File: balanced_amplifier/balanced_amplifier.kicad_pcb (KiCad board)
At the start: 2 copper layers, 100 x 100 mm, 128 parts, among them J1 Molex_SL_01x02_Male, J2 Molex_SL_01x02_Male, J3 Molex_SL_01x03_Male, J4 Molex_SL_01x02_Male, J5 Molex_SL_01x02_Male, J6 Molex_SL_01x02_Male, J7 Molex_SL_01x02_Male, U1 LM4562, U2 LM4562, U3 NE5532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

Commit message: update todo (add reminder to consider switching to horizontal connectors)
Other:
- board text added: "TODO Update date silk check pot directions change to horizontal connectors?"
- board text removed: "TODO Update date silk check pot directions"
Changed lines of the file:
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@@
-(kicad_pcb (version 20171130) (host pcbnew 5.1.2)
+(kicad_pcb (version 20171130) (host pcbnew 5.1.4)
   (general
     (thickness 1.6)
@@
     (arrow2b (pts (xy 65.200001 33.8) (xy 65.786422 34.926504)))
   )
-  (gr_text "TODO\nUpdate date silk\ncheck pot directions" (at 213.2 34.3) (layer Cmts.User)
+  (gr_text "TODO\nUpdate date silk\ncheck pot directions\nchange to horizontal connectors?" (at 213.2 34.3) (layer Cmts.User)
     (effects (font (size 1 1) (thickness 0.15)) (justify left))
   )

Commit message: move pots to be 60mm apart
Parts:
- moved RV1 3.54 mm to (93.7, 116.8)
- moved RV2 3.46 mm to (153.7, 116.8)
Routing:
- net Net-(C26-Pad2): track 89.9 -> 132.0 mm
- net Net-(C22-Pad1): track 30.3 -> 64.9 mm
- net Net-(C15-Pad2): track 20.8 -> 37.7 mm
- net Net-(C21-Pad1): track 43.8 -> 60.0 mm
- net Net-(C28-Pad1): track 57.7 -> 45.2 mm
- net Net-(C33-Pad2): track 66.0 -> 60.8 mm
- net Net-(C29-Pad1): track 15.5 -> 18.4 mm
- net Net-(RV1-Pad5): track 16.9 -> 15.0 mm
- net Net-(C7-Pad2): track 27.5 -> 29.3 mm

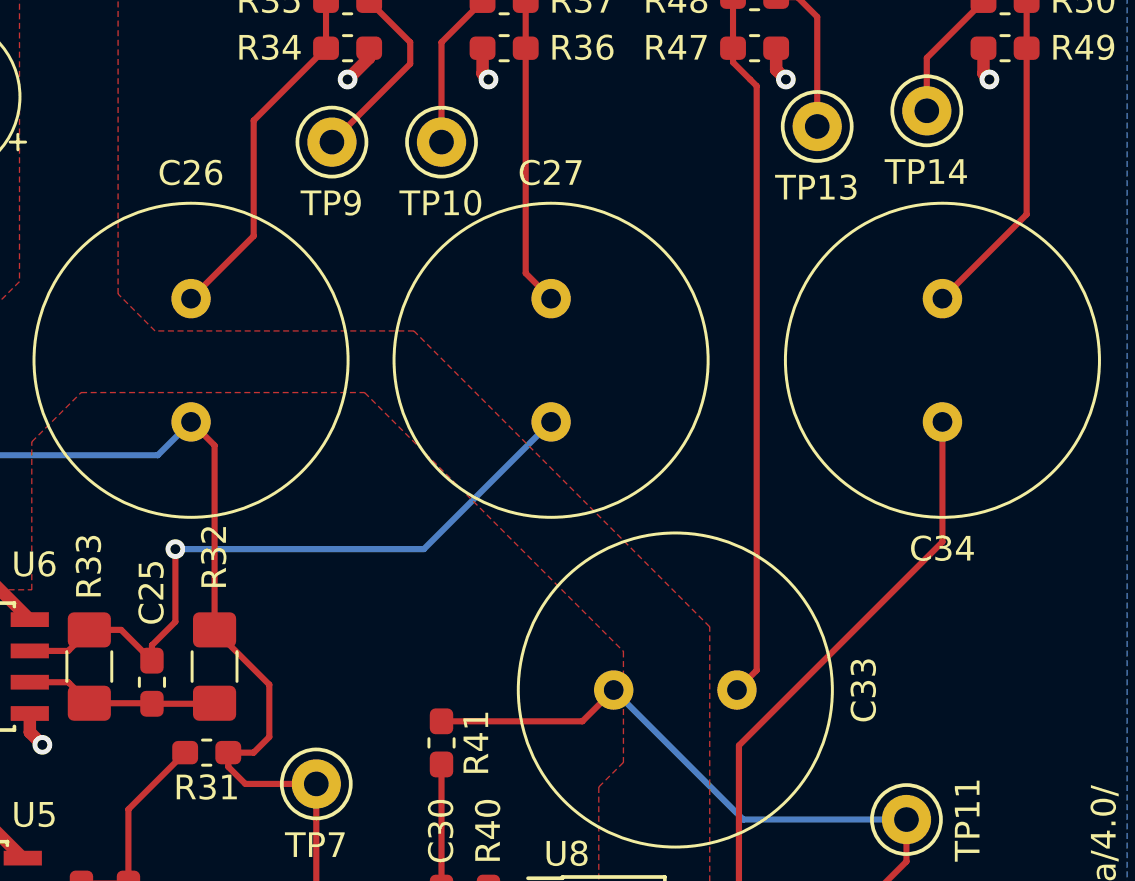
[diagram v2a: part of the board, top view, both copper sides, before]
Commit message: update footprint references for pots and output caps
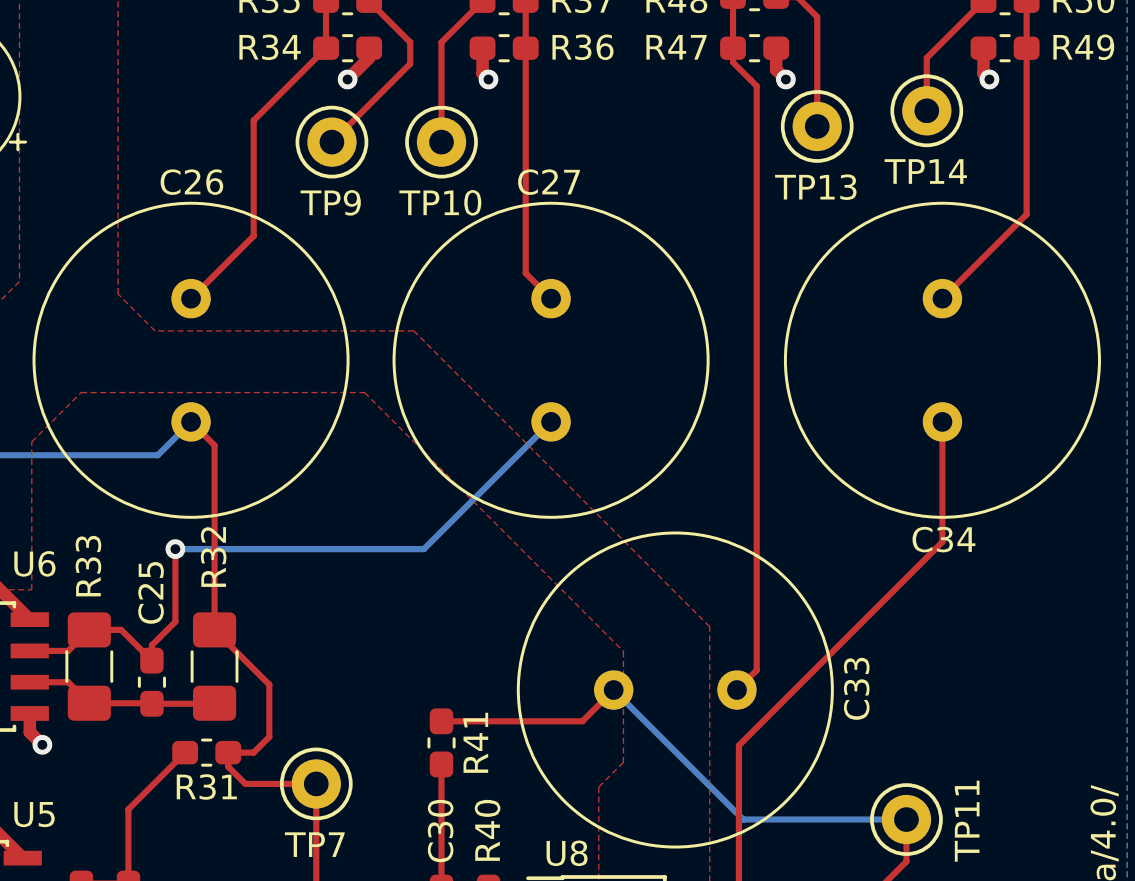
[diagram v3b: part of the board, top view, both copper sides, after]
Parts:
- C26, C27, C33, C34: footprint Capacitor_THT:C_Radial_D12.5mm_H25.0mm_P5.00mm -> Capacitor_THT:C_Radial_D12.5mm_H20.0mm_P5.00mm
- RV1, RV2: footprint Potentiometer_THT_custom:Potentiometer_Bourns_91A2x-x28-xxx_Dual_Horizontal -> Potentiometer_THT_gkeeth:Potentiometer_Bourns_91A2x-x28-xxx_Dual_Horizontal

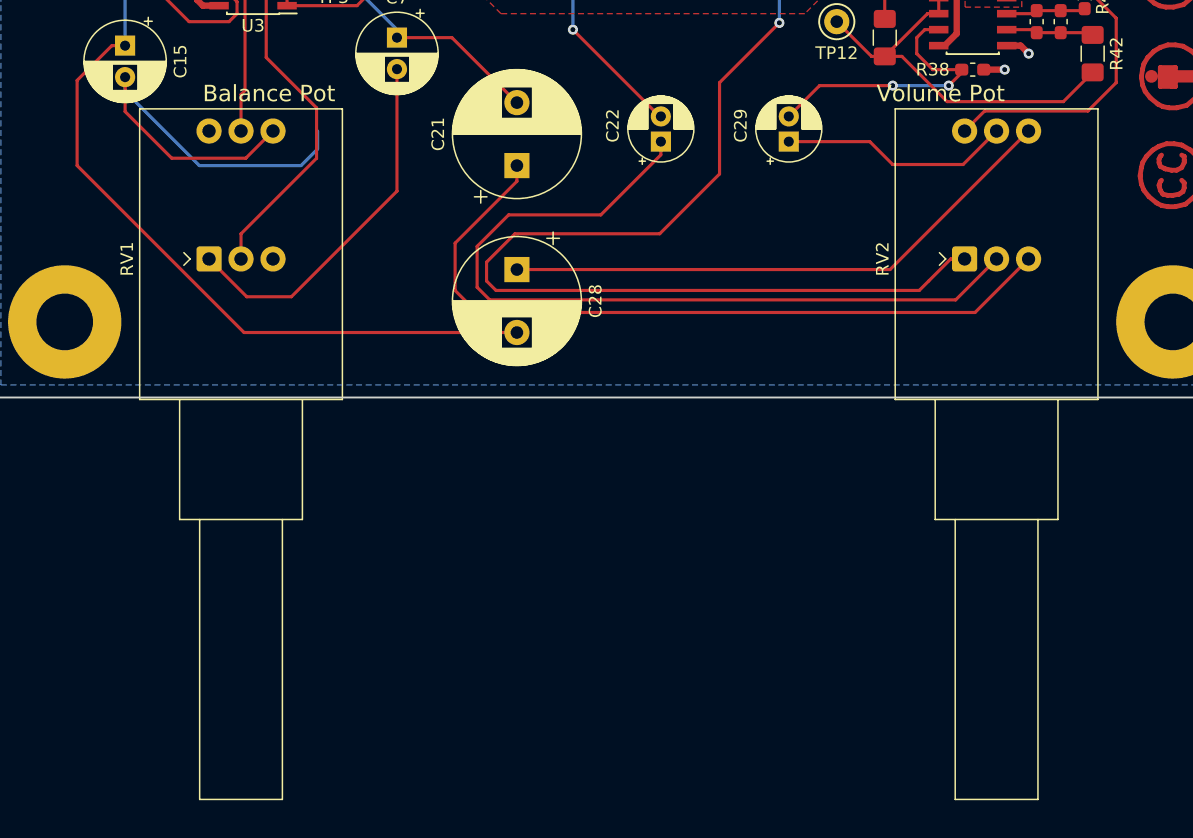
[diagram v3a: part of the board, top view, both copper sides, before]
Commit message: move pots 1mm further beyond board edge
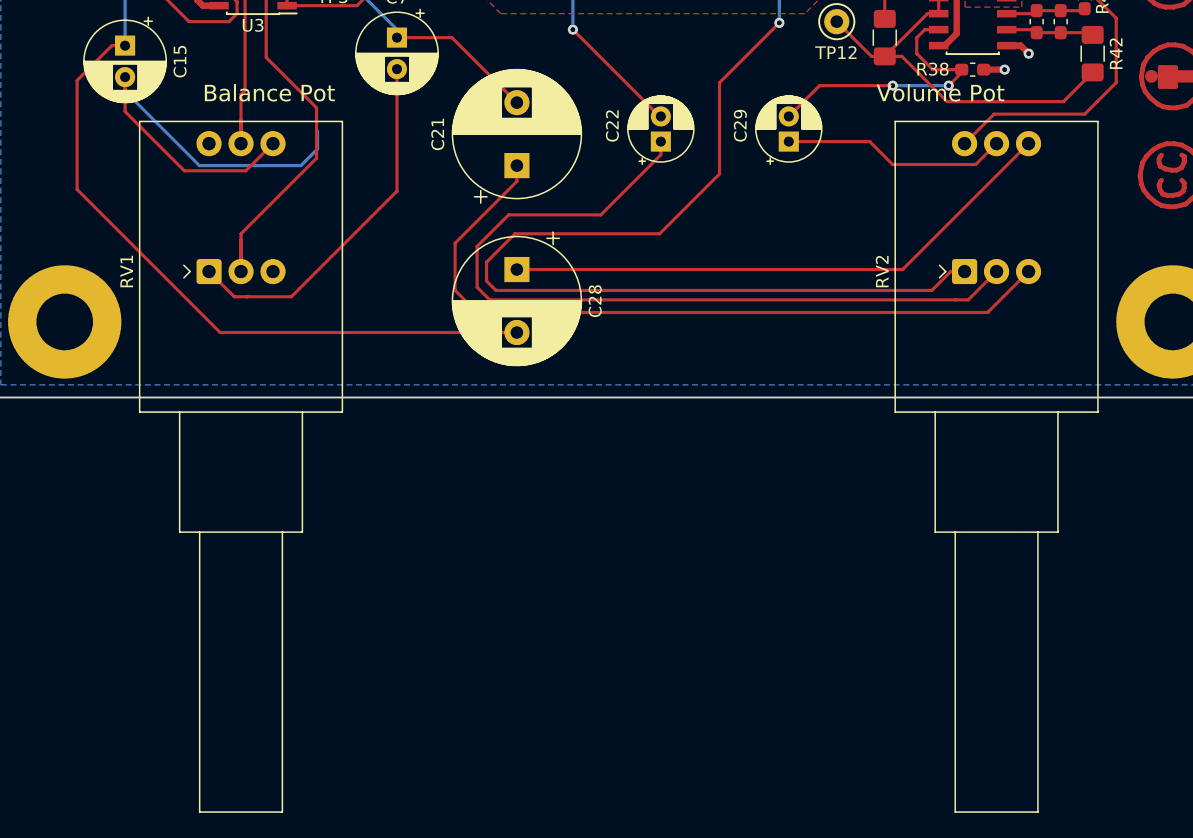
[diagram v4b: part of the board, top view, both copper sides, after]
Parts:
- moved RV1 1.00 mm to (93.7, 117.8)
- moved RV2 1.00 mm to (153.7, 117.8)
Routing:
- net Net-(RV1-Pad2): track 27.8 -> 30.3 mm
- net Net-(RV1-Pad5): track 15.0 -> 16.9 mm
- net /volume_control/left_in: track 74.3 -> 75.4 mm

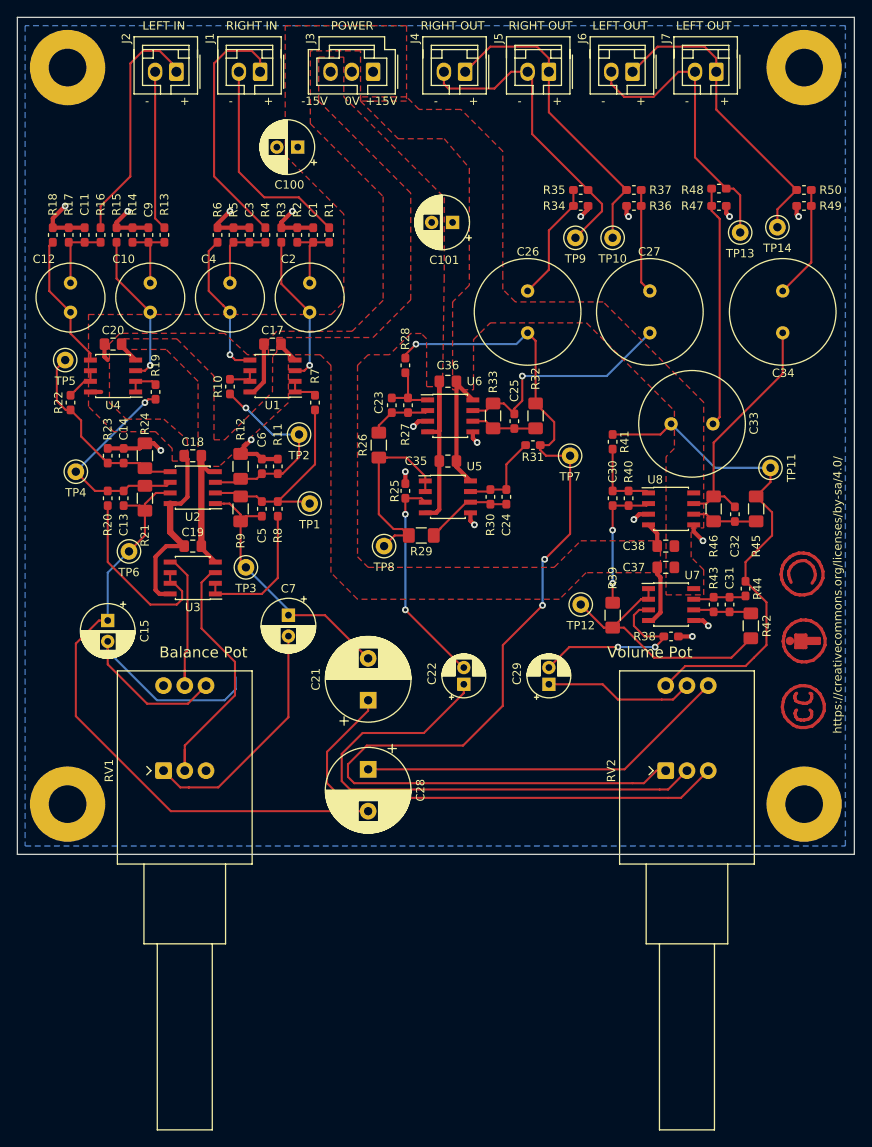
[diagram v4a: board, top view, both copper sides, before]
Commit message: Finalize layout for rev1
- switch to smaller M3 holes
- move input/output/power connectors to bottom of board for better
accessibility in enclosure
- change power planes to simple traces. Planes were unnecessary.
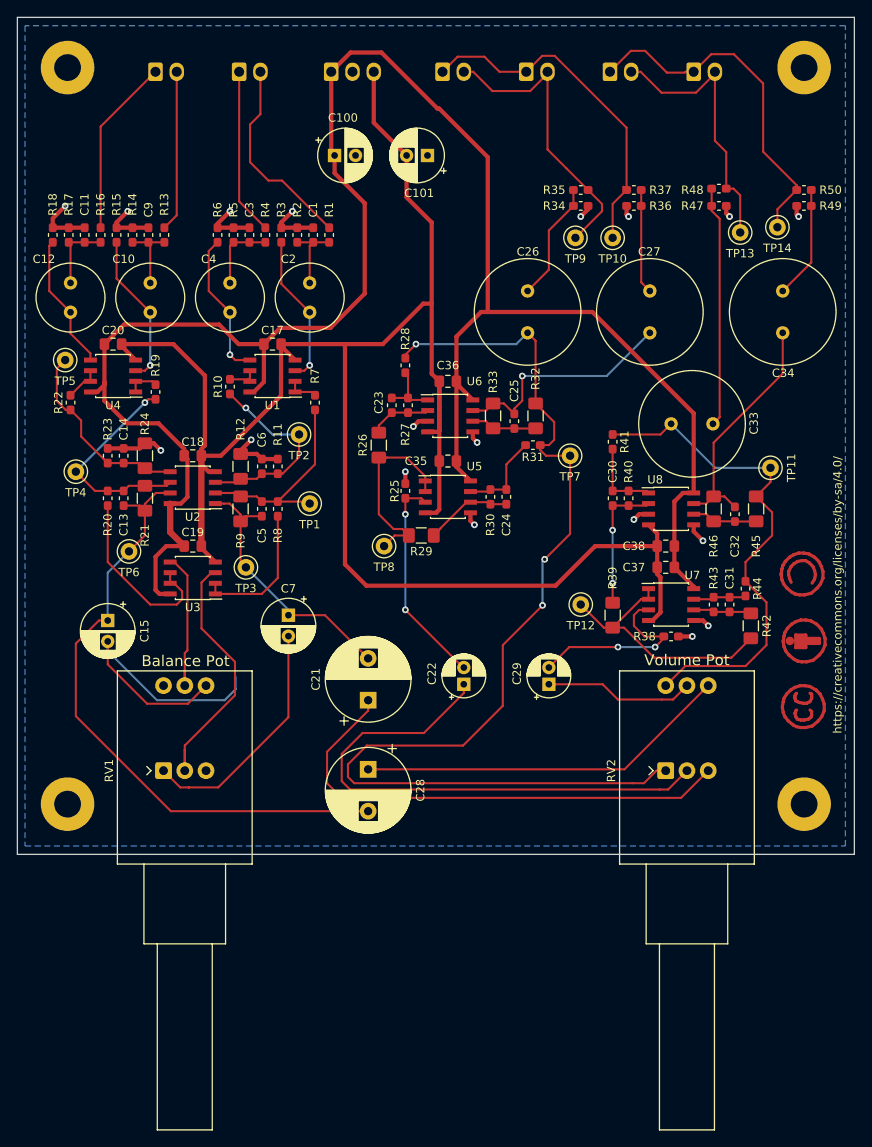
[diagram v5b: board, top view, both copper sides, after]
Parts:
- H1, H2, H3, H4: footprint MountingHole:MountingHole_4.5mm_Pad -> MountingHole:MountingHole_3.2mm_M3_Pad
- J1, J2, J3, J4, J5, J6, J7: moved to B.Cu
- moved C101 8.54 mm to (125.2, 44.3)
- moved J3 5.00 mm to (113.7, 34.3), turned to 0 degrees
- moved C100 4.51 mm to (114.1, 44.3), turned to 0 degrees
- moved J4 2.70 mm to (127.0, 34.3), turned to 0 degrees
- moved J5 2.70 mm to (137.0, 34.3), turned to 0 degrees
- moved J6 2.70 mm to (147.0, 34.3), turned to 0 degrees
- moved J7 2.70 mm to (157.0, 34.3), turned to 0 degrees
- moved J1 2.50 mm to (102.7, 34.3), turned to 0 degrees
- moved J2 2.50 mm to (92.7, 34.3), turned to 0 degrees
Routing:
- net VCC: track 49.3 -> 238.3 mm
- net VEE: track 57.4 -> 226.7 mm
- net /right_in_hot: track 30.2 -> 19.9 mm
- net /left_in_hot: track 28.5 -> 21.3 mm
- net /left_out_hot: track 36.9 -> 42.6 mm
- net /right_out_hot: track 38.4 -> 42.2 mm
- net /left_out_cold: track 35.4 -> 33.3 mm
- net /right_in_cold: track 25.5 -> 24.0 mm
- net /right_out_cold: track 37.3 -> 35.9 mm
- removed copper zone on F.Cu, net VCC
- removed copper zone on F.Cu, net VEE
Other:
- board text added: "Balanced Amplifier rev1 Preamp 2019 G. Keeth 2019-09-28"
- board text added: "TODO check pot directions"
- board text removed: "Balanced Amplifier rev1 Preamp 2019 G. Keeth 2019-06-19"
- board text removed: "TODO Update date silk check pot directions change to horizontal connectors?"

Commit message: remove TODO from balanced amplifier
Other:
- board text removed: "TODO check pot directions"
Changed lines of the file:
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@@
   (general
     (thickness 1.6)
-    (drawings 15)
+    (drawings 14)
     (tracks 612)
     (zones 0)
@@
     (arrow2b (pts (xy 65.200001 33.8) (xy 65.786422 34.926504)))
   )
-  (gr_text "TODO\ncheck pot directions" (at 213.2 34.3) (layer Cmts.User)
-    (effects (font (size 1 1) (thickness 0.15)) (justify left))
-  )
   (gr_text "Volume Pot" (at 156.2 104.6) (layer F.SilkS)
